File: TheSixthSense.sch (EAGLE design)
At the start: 84 parts, among them Q1 IRLML 5203, Q10 Si2302CDS, Q2 PDTC114YT, Q3 Si2302CDS, Q4 Si2302CDS, Q5 Si2302CDS, Q6 Si2302CDS, Q7 Si2302CDS, Q8 Si2302CDS, Q9 Si2302CDS, U1 ATXMEGA32E5-AU, U2 MCP73831, U3 LSM303D, U4 MCP1700T-2502E/TT, U6 KPGA-1602CGC-KA, U7 KPGA-1602CGC-KA

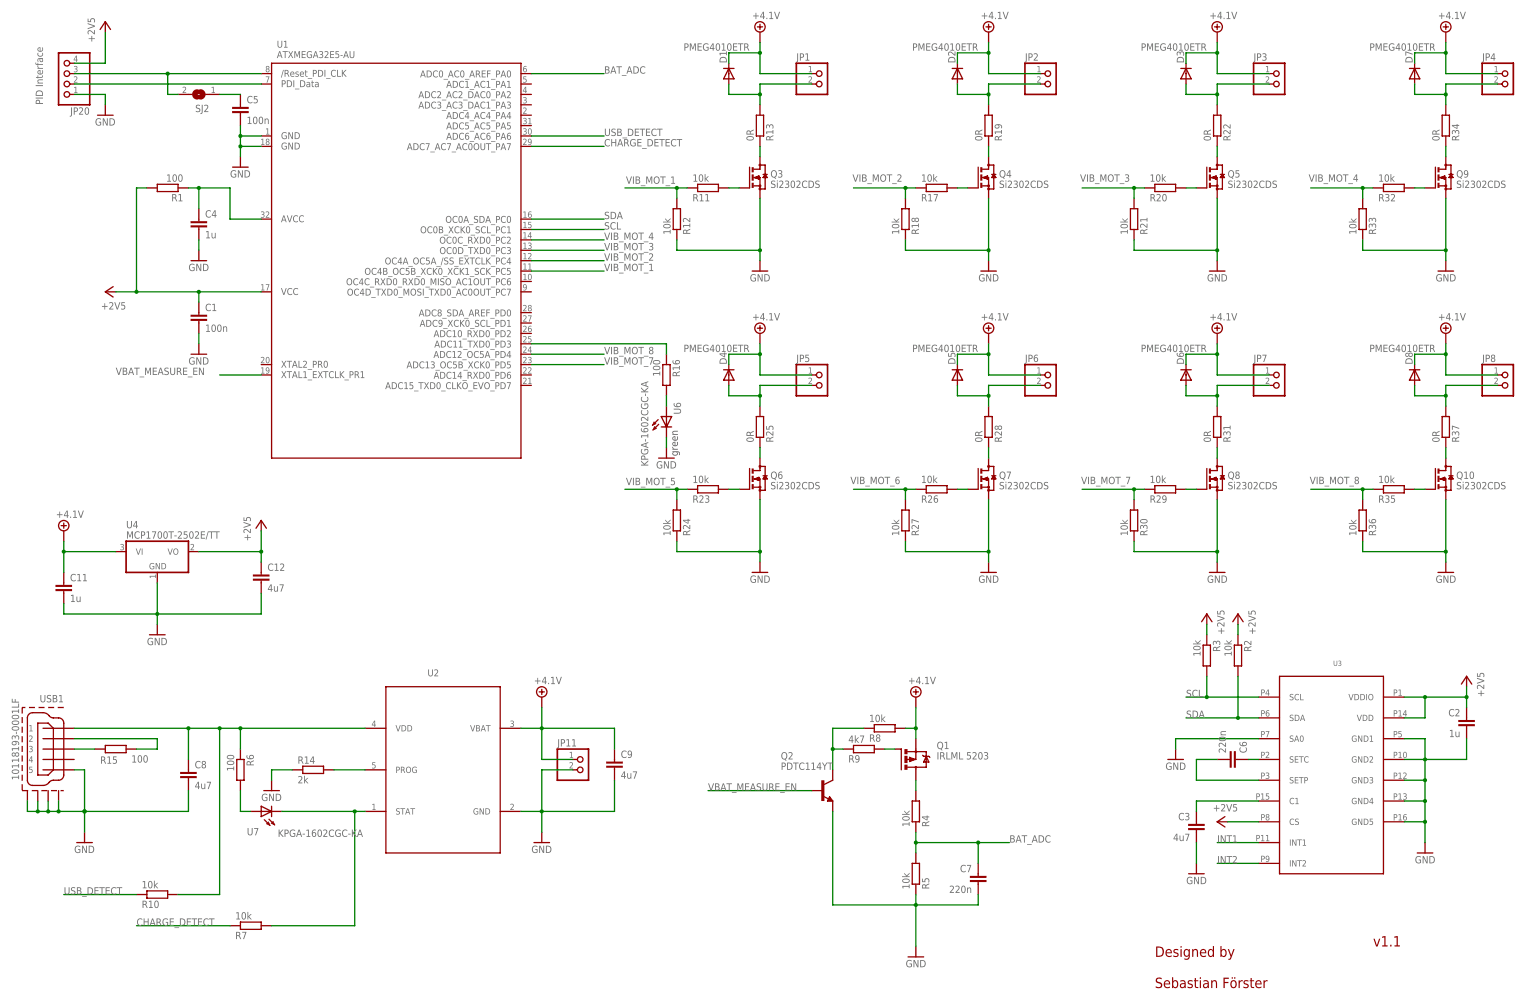
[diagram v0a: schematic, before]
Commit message: New 8 motor support! - adding motor 5&6: µC <-> Mosfets
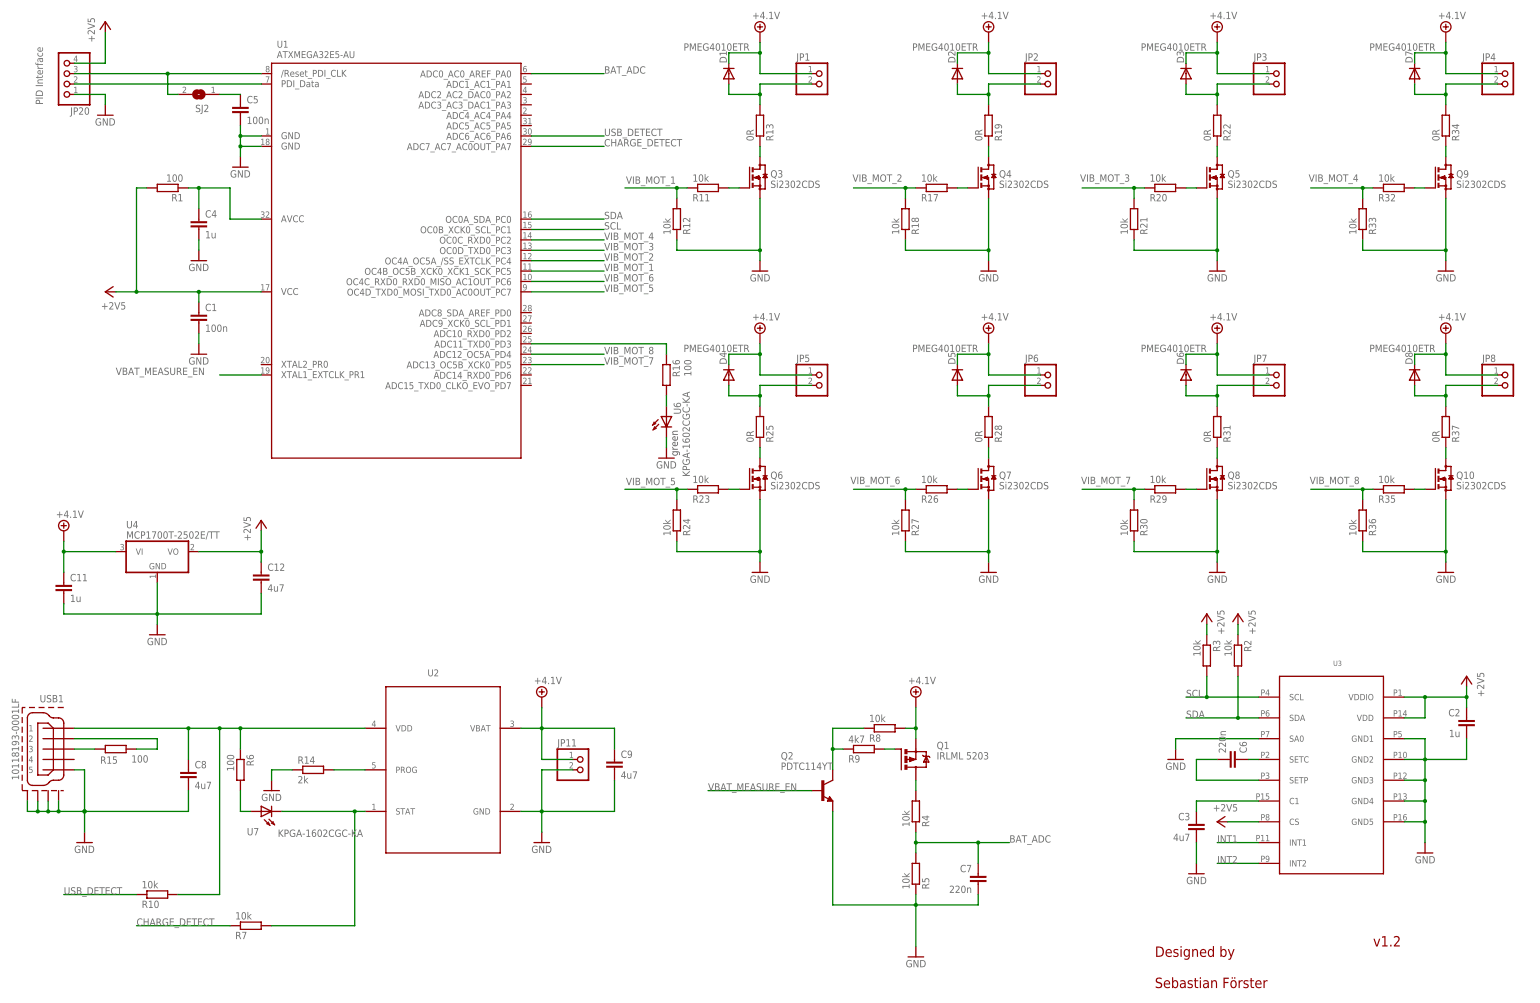
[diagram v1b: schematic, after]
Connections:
- net VIB_MOT_5: now also U1.PC7
- net VIB_MOT_6: now also U1.PC6
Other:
- note added: "v1.2"
- note removed: "Feel free to connect them and do a Software PWM to support 8 drivers."
- note removed: "Motor 5 & 6 FETs are not connected to the µC because of a design bug with I2C lines."
- note removed: "v1.1"
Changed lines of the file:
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@@
 <text x="292.1" y="10.16" size="2.54" layer="94">Sebastian Förster</text>
 <text x="173.736" y="146.558" size="1.778" layer="97" rot="R270">green</text>
-<text x="345.44" y="20.32" size="2.54" layer="94">v1.1</text>
+<text x="345.44" y="20.32" size="2.54" layer="94">v1.2</text>
 <text x="104.14" y="40.64" size="1.778" layer="104">MCP73831T-2DCI/OT</text>
 <text x="322.58" y="35.56" size="1.778" layer="104">LSM303D</text>
-<text x="170.18" y="104.14" size="2.1844" layer="104">Motor 5 &amp; 6 FETs are not connected to the µC because of a design bug with I2C lines.</text>
-<text x="170.18" y="99.06" size="2.1844" layer="104">Feel free to connect them and do a Software PWM to support 8 drivers.</text>
 <text x="142.24" y="172.72" size="2.1844" layer="104">(I2C Slave only on this Pins!)</text>
 </plain>
@@
 <instance part="GND5" gate="1" x="233.68" y="17.78" rot="MR0"/>
 <instance part="R8" gate="G$1" x="226.06" y="73.66" rot="MR180"/>
-<instance part="R16" gate="G$1" x="172.72" y="160.02" rot="R270"/>
+<instance part="R16" gate="G$1" x="172.72" y="160.02" smashed="yes" rot="R270">
+<attribute name="NAME" x="174.2186" y="163.83" size="1.778" layer="95" rot="R270"/>
+<attribute name="VALUE" x="177.038" y="163.83" size="1.778" layer="96" rot="R270"/>
+</instance>
 <instance part="U6" gate="G$1" x="172.72" y="149.86" smashed="yes">
 <attribute name="NAME" x="176.276" y="150.368" size="1.778" layer="95" rot="R90"/>
-<attribute name="VALUE" x="168.275" y="137.668" size="1.778" layer="96" rot="R90"/>
+<attribute name="VALUE" x="178.435" y="135.128" size="1.778" layer="96" rot="R90"/>
 </instance>
 <instance part="SJ2" gate="1" x="58.42" y="228.6" rot="R180"/>
@@
 <label x="162.814" y="133.096" size="1.778" layer="95"/>
 </segment>
+<segment>
+<pinref part="U1" gate="G$1" pin="PC7"/>
+<wire x1="139.7" y1="180.34" x2="157.48" y2="180.34" width="0.1524" layer="91"/>
+<label x="157.48" y="180.34" size="1.778" layer="95"/>
+</segment>
 </net>
 <net name="N$32" class="0">
@@
 <label x="217.678" y="133.35" size="1.778" layer="95"/>
 </segment>
-</net>
+<segment>
+<pinref part="U1" gate="G$1" pin="PC6"/>
+<wire x1="139.7" y1="182.88" x2="157.48" y2="182.88" width="0.1524" layer="91"/>
+<label x="157.48" y="182.88" size="1.778" layer="95"/>
+</segment>
+</net>

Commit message: - new version v1.3 - add a push button - add a fuse - add a switch to disconnect the battery - add a new motor connector
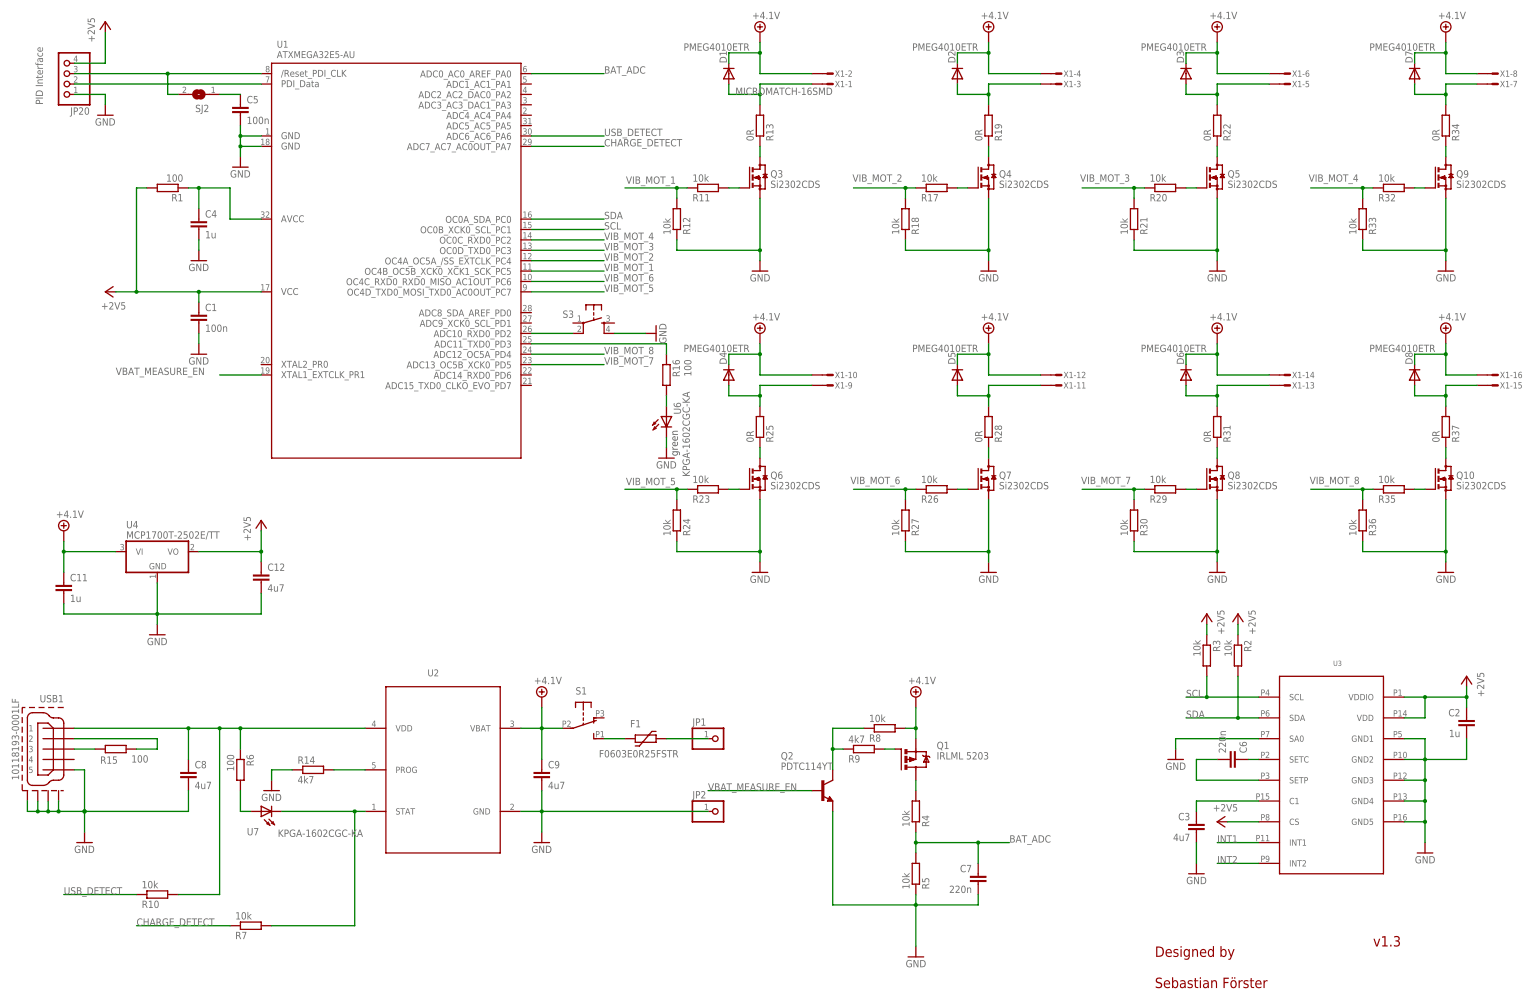
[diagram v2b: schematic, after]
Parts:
- removed JP11, JP3, JP4, JP5, JP6, JP7, JP8: (no value), pinhead:PINHD-1X2
- added F1: F0603E0R25FSTR, ptc-littlefuse:PMS1812
- added S1: ALPSSSSS811101, ALP_Switch:ALPSSSSS811101
- added S3: (no value), smd_right_switch:10-XX
- added X1: MICROMATCH-16SMD, Con-amp-micromatch:MICROMATCH-16SMD
- JP1, JP2: device pinhead:PINHD-1X2 -> pinhead:PINHD-1X1
- R14: value 2k -> 4k7
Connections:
- new net N$35: F1.2, JP1.1
- new net N$36: S3.P1, U1.PD2
- new net N$5: F1.1, S1.S
- net +4.1V: now also S1.P, X1-10.S, X1-12.S, X1-14.S, X1-16.S, X1-2.S, X1-4.S, X1-6.S, X1-8.S; no longer JP1.1, JP11.1, JP2.1, JP3.1, JP4.1, JP5.1, JP6.1, JP7.1, JP8.1
- net GND: now also JP2.1, S3.S1; no longer JP11.2
- net N$17: now also X1-1.S; no longer JP1.2
- net N$21: now also X1-3.S; no longer JP2.2
- net N$24: now also X1-5.S; no longer JP3.2
- net N$28: now also X1-9.S; no longer JP5.2
- net N$31: now also X1-11.S; no longer JP6.2
- net N$34: now also X1-13.S; no longer JP7.2
- net N$45: now also X1-7.S; no longer JP4.2
- net N$48: now also X1-15.S; no longer JP8.2
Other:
- note added: "v1.3"
- note removed: "(I2C Slave only on this Pins!)"
- note removed: "v1.2"
- moved on the sheet: C9
